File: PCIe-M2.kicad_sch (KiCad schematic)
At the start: 10 parts, among them J7 Bus_M.2_Socket_E, M1 M.2 Solder Nut, M2 M.2 Solder Nut, M3 M.2 Solder Nut, M4 M.2 Solder Nut, M5 M.2 Screw, U4 ASEK-32.768KHZ-L-R-T

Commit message: change cad data
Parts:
- D9: renamed from D8; footprint LED_SMD:LED_0603_1608Metric -> LED_SMD:LED_0603_1608Metric_Pad1.05x0.95mm_HandSolder
- renumbered C12 to C26, R41 to R50, U4 to U6
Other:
- moved on the sheet: C26, D9, J7, R50, U6

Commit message: remove efuse
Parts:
- renumbered C26 to C22, R50 to R49
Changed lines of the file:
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@@
 		(on_board yes)
 		(dnp no)
-		(property "Reference" "C26"
+		(property "Reference" "C22"
 			(at 221.361 151.2316 0)
 			(effects
@@
 			(project "mainboard4"
 				(path "/dd07ab80-a59c-44f4-ac7d-849e21e1384e/0c30b420-9464-42a2-80c6-fb3967709830"
-					(reference "C26")
+					(reference "C22")
 					(unit 1)
 				)
@@
 		(on_board yes)
 		(dnp no)
-		(property "Reference" "R50"
+		(property "Reference" "R49"
 			(at 168.148 97.8916 0)
 			(effects
@@
 			(project "mainboard4"
 				(path "/dd07ab80-a59c-44f4-ac7d-849e21e1384e/0c30b420-9464-42a2-80c6-fb3967709830"
-					(reference "R50")
+					(reference "R49")
 					(unit 1)
 				)

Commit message: add sata capacitor
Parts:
- added C26: 0.01uF, Capacitor_SMD:C_0603_1608Metric, symbol Device:C
- added C27, C28, C29: 0.1uF, Capacitor_SMD:C_0603_1608Metric, symbol Device:C
- renumbered C22 to C31, D9 to D10, R49 to R50
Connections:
- net +3.3V: now also C26.1, C27.1, C28.1, C29.1
- net GND: now also C26.2, C27.2, C28.2, C29.2

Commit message: add logp
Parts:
- renumbered R50 to R47
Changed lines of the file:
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@@
 	(label "M2_3v3"
 		(at 162.56 181.61 0)
-		(fields_autoplaced yes)
 		(effects
 			(font
@@
 		(shape input)
 		(at 104.14 50.8 180)
-		(fields_autoplaced yes)
 		(effects
 			(font
@@
 		(shape bidirectional)
 		(at 107.95 83.82 180)
-		(fields_autoplaced yes)
 		(effects
 			(font
@@
 		(shape input)
 		(at 100.33 132.08 180)
-		(fields_autoplaced yes)
 		(effects
 			(font
@@
 		(shape output)
 		(at 104.14 66.04 180)
-		(fields_autoplaced yes)
 		(effects
 			(font
@@
 		(shape input)
 		(at 104.14 63.5 180)
-		(fields_autoplaced yes)
 		(effects
 			(font
@@
 		(shape input)
 		(at 104.14 60.96 180)
-		(fields_autoplaced yes)
 		(effects
 			(font
@@
 		(shape bidirectional)
 		(at 107.95 86.36 180)
-		(fields_autoplaced yes)
 		(effects
 			(font
@@
 		(shape input)
 		(at 100.33 129.54 180)
-		(fields_autoplaced yes)
 		(effects
 			(font
@@
 		(shape output)
 		(at 104.14 55.88 180)
-		(fields_autoplaced yes)
 		(effects
 			(font
@@
 		(shape output)
 		(at 104.14 53.34 180)
-		(fields_autoplaced yes)
 		(effects
 			(font
@@
 		(shape output)
 		(at 104.14 68.58 180)
-		(fields_autoplaced yes)
 		(effects
 			(font
@@
 		(on_board yes)
 		(dnp no)
-		(property "Reference" "R50"
+		(property "Reference" "R47"
 			(at 168.148 97.8916 0)
 			(effects
@@
 			(project "mainboard4"
 				(path "/dd07ab80-a59c-44f4-ac7d-849e21e1384e/0c30b420-9464-42a2-80c6-fb3967709830"
-					(reference "R50")
-					(unit 1)
-				)
+					(reference "R47")
+					(unit 1)
+				)

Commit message: end route
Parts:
- renumbered C31 to C27, C27 to C30, C26 to C31, C28 to C32, C29 to C33
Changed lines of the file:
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@@
 		(on_board yes)
 		(dnp no)
-		(property "Reference" "C27"
+		(property "Reference" "C30"
 			(at 207.264 46.228 0)
 			(effects
@@
 			(project "mainboard4"
 				(path "/dd07ab80-a59c-44f4-ac7d-849e21e1384e/0c30b420-9464-42a2-80c6-fb3967709830"
-					(reference "C27")
+					(reference "C30")
 					(unit 1)
 				)
@@
 		(on_board yes)
 		(dnp no)
-		(property "Reference" "C31"
+		(property "Reference" "C27"
 			(at 221.361 151.2316 0)
 			(effects
@@
 			(project "mainboard4"
 				(path "/dd07ab80-a59c-44f4-ac7d-849e21e1384e/0c30b420-9464-42a2-80c6-fb3967709830"
-					(reference "C31")
+					(reference "C27")
 					(unit 1)
 				)
@@
 		(on_board yes)
 		(dnp no)
-		(property "Reference" "C29"
+		(property "Reference" "C33"
 			(at 174.498 50.038 0)
 			(effects
@@
 			(project "mainboard4"
 				(path "/dd07ab80-a59c-44f4-ac7d-849e21e1384e/0c30b420-9464-42a2-80c6-fb3967709830"
-					(reference "C29")
+					(reference "C33")
 					(unit 1)
 				)
@@
 		(on_board yes)
 		(dnp no)
-		(property "Reference" "C26"
+		(property "Reference" "C31"
 			(at 195.58 39.624 0)
 			(effects
@@
 			(project "mainboard4"
 				(path "/dd07ab80-a59c-44f4-ac7d-849e21e1384e/0c30b420-9464-42a2-80c6-fb3967709830"
-					(reference "C26")
+					(reference "C31")
 					(unit 1)
 				)
@@
 		(on_board yes)
 		(dnp no)
-		(property "Reference" "C28"
+		(property "Reference" "C32"
 			(at 187.96 43.942 0)
 			(effects
@@
 			(project "mainboard4"
 				(path "/dd07ab80-a59c-44f4-ac7d-849e21e1384e/0c30b420-9464-42a2-80c6-fb3967709830"
-					(reference "C28")
-					(unit 1)
-				)
+					(reference "C32")
+					(unit 1)
+				)

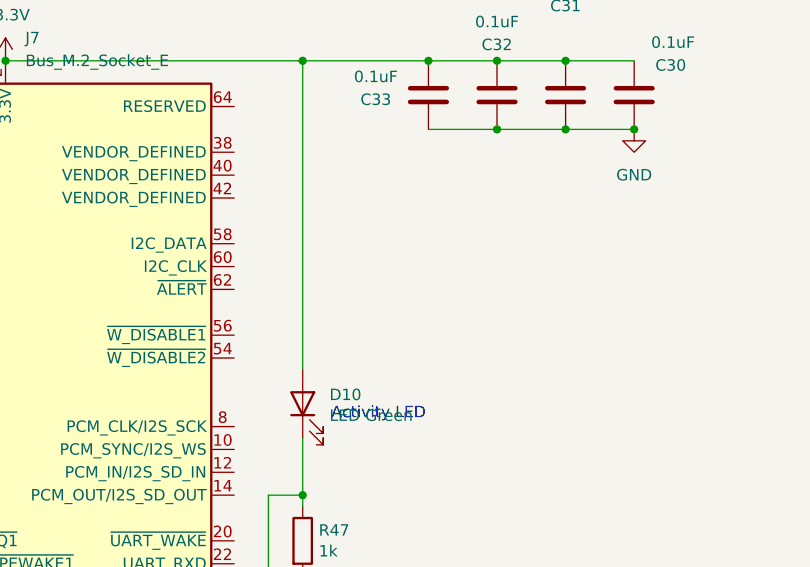
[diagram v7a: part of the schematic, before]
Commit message: add disable pin pullup
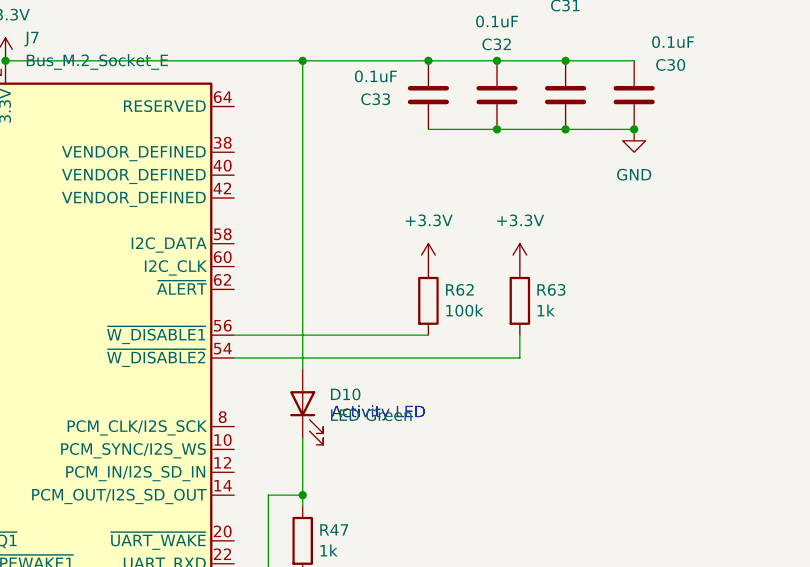
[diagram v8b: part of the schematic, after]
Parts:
- added R62: 100k, Resistor_SMD:R_0603_1608Metric_Pad0.98x0.95mm_HandSolder, symbol Device:R
- added R63: 1k, Resistor_SMD:R_0603_1608Metric_Pad0.98x0.95mm_HandSolder, symbol Device:R
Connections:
- net +3.3V: now also R62.1, R63.1
- net at J7.54 (~{W_DISABLE2}): now also R63.2
- net at J7.56 (~{W_DISABLE1}): now also R62.2
